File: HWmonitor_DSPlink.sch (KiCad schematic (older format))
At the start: 10 parts

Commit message: Schematic drawn!
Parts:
- removed J?: USB_B_Mini, symbol Connector:USB_B_Mini
- removed U?: FT232RL, Package_SO:SSOP-28_5.3x10.2mm_P0.65mm, symbol Interface_USB:FT232RL
- added C1, C10, C11, C12, C13, C14, C19, C20, C21, C22, C23, C28, C29, C30, C31, C32, C33, C34, C35, C5, C6: 100nF/50V, symbol Device:C
- added C15, C16, C17, C18, C2, C9: 10uF/16V, symbol Device:C
- added C24, C25, C26, C27: 68pF/50V, symbol Device:C
- added C3, C4, C7, C8: NM, symbol Device:C
- added D1, D3, D6, D7, D8: BAV99, Package_TO_SOT_SMD:SOT-23, symbol Diode:BAV99
- added D10, D5, D9: LED, symbol Device:LED
- added D11, D12, D2: D_Schottky, symbol Device:D_Schottky
- added D4: D_Zener, symbol Device:D_Zener
- added J1: USB_B_Mini, symbol Connector:USB_B_Mini
- added J3, J4, J5, J6: Conn_Coaxial, symbol Connector:Conn_Coaxial
- added L1: 0603, symbol #MyLibrary:Ferrite_Bead
- added R1, R11, R12, R13, R14, R2, R23, R24, R25, R26, R4, R5, R6, R7: 10R, symbol Device:R
- added R10: 750R, symbol Device:R
- added R15, R16, R17, R18, R19, R20, R21, R22: 10k, symbol Device:R
- added R3: 27R, symbol Device:R
- added R8, R9: 270R, symbol Device:R
- added U1: FT232RL, Package_SO:SSOP-28_5.3x10.2mm_P0.65mm, symbol Interface_USB:FT232RL
- added U10, U11, U9: OPA197xDBV, Package_TO_SOT_SMD:SOT-23-5, symbol Amplifier_Operational:OPA197xDBV
- added U5: TL431DBZ, Package_TO_SOT_SMD:SOT-23, symbol Reference_Voltage:TL431DBZ
- gave numbers to parts that had none: 8
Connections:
- net at T1.1: now also U4.3 (D2)
- net +5VA: now reaches T1.2
- net +5VA: now also U3.13 (EN2), U3.16 (VCC2), U4.2 (VCC), C1.1, C10.1, C12.1, C9.2, L1.2, R8.1, R9.1, U1.20 (VCC), U1.4 (VCCIO)
- net at T1.3: now also U4.1 (D1)
- net at T1.4: now also D12.1 (K)
- net GND: now reaches T1.5
- net GND: now also U2.15 (GND2), U2.9 (GND2), U6.7 (GND), U7.1 (GND), C11.2, C13.1, C14.1, C15.1, C16.1, C17.2, C18.1, C19.2, C20.1, C21.1, C22.1, C23.1, C24.1, C25.1, C26.1, C27.1, C28.1, C29.1, C30.1, C31.1, C32.1, C33.1, C34.1, C35.1, J3.2 (Ext), J4.2 (Ext), J5.2 (Ext), J6.2 (Ext), U5.3 (A)
- net at T1.6: now also D11.2 (A)
- net GNDA: now reaches U4.4 (GND)
- net GNDA: now also U3.15 (GND2), U3.9 (GND2), U4.5 (GND), C1.2, C10.2, C12.2, C9.1, J1.4 (ID), J1.5 (GND), J1.6 (Shield), U1.18 (GND), U1.21 (GND), U1.25 (AGND), U1.26 (TEST), U1.7 (GND)
- net at J2.1 (Pin_1): now also R3.1
- net at J2.2 (Pin_2): now also R5.1
- net at J2.3 (Pin_3): now also R1.2
- net at J2.4 (Pin_4): now also R6.1
- net at J2.6 (Pin_6): now also R7.1
- net at J2.7 (Pin_7): now also R2.2
- net GNDD: now reaches J2.8 (Pin_8)
- net GNDD: now also U2.2 (GND1), U2.8 (GND1), U3.2 (GND1), U3.8 (GND1), C2.1, C3.1, C4.1, C5.1, C6.1, C7.1, C8.1, D1.1 (K), D2.2 (A), D3.1 (K), D4.2 (A), D5.1 (K), D6.1 (K), D7.1 (K), D8.1 (K)
- net at U8.1: now also R19.1, R23.2
- net -7.5V: now reaches U8.2 (V-)
- net -7.5V: now also C17.1, C28.2, C29.2, C30.2, C31.2, D12.2 (A), U10.2 (V-), U11.2 (V-), U9.2 (V-)
- net at U8.3 (+): now also C24.2, R11.1
- net at U8.4 (-): now also R15.1, R19.2
- net +7.5V: now reaches U8.5 (V+)
- net +7.5V: now also U7.2 (VIN), C14.2, C16.2, C32.2, C33.2, C34.2, C35.2, D11.1 (K), U10.5 (V+), U11.5 (V+), U9.5 (V+)
- net VD: now reaches U3.1 (VCC1)
- net VD: now also U2.1 (VCC1), U3.4 (EN1), C2.2, C5.2, C6.2, D1.2 (A), D2.1 (K), D3.2 (A), D4.1 (K), D6.2 (A), D7.2 (A), D8.2 (A), R3.2, R4.1
- net RXD: now reaches U3.11 (OUTB)
- net RXD: now also U1.5 (RXD)
- net TXD: now reaches U3.12 (INA)
- net TXD: now also U1.1 (TXD)
- net RXD_DSP: now reaches U3.5 (OUTA)
- net RXD_DSP: now also D1.3 (K), R2.1
- net TXD_DSP: now reaches U3.6 (INB)
- net TXD_DSP: now also C8.2, D3.3 (K), R7.2
- net +5V: now reaches U2.10 (EN2)
- net +5V: now also U2.16 (VCC2), U6.1 (VDD), U7.3 (VOUT), C11.1, C18.2, C19.1, R10.2
- net SYNC: now reaches U2.12 (OUTC)
- net SYNC: now also U6.10 (SYNC)
- net SCLK: now reaches U2.13 (OUTB)
- net SCLK: now also U6.9 (SCLK)
- net DIN: now reaches U2.14 (OUTA)
- net DIN: now also U6.8 (DIN)
- net DIN_DSP: now reaches U2.3 (INA)
- net DIN_DSP: now also C3.2, D7.3 (K), R1.1
- net SCLK_DSP: now reaches U2.4 (INB)
- net SCLK_DSP: now also C4.2, D8.3 (K), R5.2
- net SYNC_DSP: now reaches U2.5 (INC)
- net SYNC_DSP: now also C7.2, D6.3 (K), R6.2
- net VOUTA: now reaches U6.2 (VOUTA)
- net VOUTA: now also R11.2, R12.2, R13.2, R14.2
- net VOUTB: now reaches U6.3 (VOUTB)
- net VOUTC: now reaches U6.4 (VOUTC)
- net REF2.5V: now reaches U6.5 (REFIN)
- net REF2.5V: now also C13.2, C15.2, C20.2, C21.2, C22.2, C23.2, R10.1, R15.2, R16.2, R17.2, R18.2, U5.1 (K), U5.2 (REF)
- net VOUTD: now reaches U6.6 (VOUTD)
- new net: J3.1 (In), R23.1
- new net: D5.2 (A), R4.2
- new net: J1.3 (D+), U1.15 (USBD+)
- new net: J1.2 (D-), U1.16 (USBD-)
- new net: J1.1 (VBUS), L1.1
- new net: D9.2 (A), R8.2
- new net: D10.2 (A), R9.2
- new net: R20.1, R24.2, U9.1
- new net: C25.2, R12.1, U9.3 (+)
- new net: R16.1, R20.2, U9.4 (-)
- new net: J4.1 (In), R24.1
- new net: R21.1, R25.2, U10.1
- new net: C26.2, R13.1, U10.3 (+)
- new net: R17.1, R21.2, U10.4 (-)
- new net: J5.1 (In), R25.1
- new net: R22.1, R26.2, U11.1
- new net: C27.2, R14.1, U11.3 (+)
- new net: R18.1, R22.2, U11.4 (-)
- new net: J6.1 (In), R26.1
- new net LED_RX: D10.1 (K), U1.22 (CBUS1)
- new net LED_TX: D9.1 (K), U1.23 (CBUS0)
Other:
- note added: "01"
- note added: "5. November 2020"
- note added: "Debug Tool"
- note added: "HWmonitor & DSPlink debug tool"
- moved on the sheet: J2, T1, U2, U3, U4, U6, U7, U8

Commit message: all footprints assigned
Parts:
- C1, C10, C11, C12, C13, C14, C19, C2, C20, C21, C22, C23, C24, C25, C26, C27, C28, C29, C3, C30, C31, C32, C33, C34, C35, C4, C5, C6, C7, C8: footprint (none) -> Capacitor_SMD:C_0603_1608Metric
- C15, C16, C17, C18, C9: footprint (none) -> Capacitor_SMD:C_0805_2012Metric
- D10, D5, D9: footprint (none) -> LED_THT:LED_D3.0mm_FlatTop
- D11, D12: footprint (none) -> Diode_SMD:D_SOD-323
- D2, D4: footprint (none) -> Diode_SMD:D_SOD-323F
- J1: footprint (none) -> Connector_USB:USB_Mini-B_Lumberg_2486_01_Horizontal
- J2: footprint (none) -> Connector_IDC:IDC-Header_2x04_P2.54mm_Vertical
- J3, J4, J5, J6: footprint (none) -> #MyLibrary:Connector_131-3701-301
- L1: footprint (none) -> Inductor_SMD:L_0603_1608Metric
- R1, R10, R11, R12, R13, R14, R15, R16, R17, R18, R19, R2, R20, R21, R22, R23, R24, R25, R26, R3, R4, R5, R6, R7, R8, R9: footprint (none) -> Resistor_SMD:R_0603_1608Metric
- T1: footprint (none) -> #MyLibrary:Wuerth_760390014
- U2, U3: footprint (none) -> #MyLibrary:SOIC-16DWW
- U4, U7: footprint (none) -> Package_TO_SOT_SMD:SOT-23-5
- U6: footprint (none) -> Package_SO:MSOP-10_3x3mm_P0.5mm

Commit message: initial placement
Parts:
- added H1, H2, H3, H4: MountingHole, MountingHole:MountingHole_3.2mm_M3, symbol Mechanical:MountingHole
- renumbered J3 to X1, J4 to X2, J5 to X3, J6 to X4
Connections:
- net VOUTA: no longer R12.2, R13.2, R14.2
- net VOUTB: now also R12.2
- net VOUTC: now also R13.2
- net VOUTD: now also R14.2
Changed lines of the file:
@@
 	13400 1200 13400 1450
 $Comp
-L Connector:Conn_Coaxial J3
+L Connector:Conn_Coaxial X1
 U 1 1 5FA672A6
 P 14850 1750
-F 0 "J3" H 14950 1725 50  0000 L CNN
+F 0 "X1" H 14950 1725 50  0000 L CNN
 F 1 "Conn_Coaxial" H 14950 1634 50  0000 L CNN
 F 2 "#MyLibrary:Connector_131-3701-301" H 14850 1750 50  0001 C CNN
@@
 	5400 2250 5400 2400
 Wire Wire Line
-	5450 1950 5100 1950
-Wire Wire Line
 	5100 1950 5100 2050
 Wire Wire Line
@@
 Wire Wire Line
 	5100 1950 3950 1950
-Connection ~ 5100 1950
 Wire Wire Line
 	3950 1850 4750 1850
@@
 	12150 3750 11850 3750
 Text Label 11850 3750 0    50   ~ 0
-VOUTA
+VOUTB
 Wire Wire Line
 	14500 3850 14650 3850
@@
 	13400 3300 13400 3550
 $Comp
-L Connector:Conn_Coaxial J4
+L Connector:Conn_Coaxial X2
 U 1 1 61F80535
 P 14850 3850
-F 0 "J4" H 14950 3825 50  0000 L CNN
+F 0 "X2" H 14950 3825 50  0000 L CNN
 F 1 "Conn_Coaxial" H 14950 3734 50  0000 L CNN
 F 2 "#MyLibrary:Connector_131-3701-301" H 14850 3850 50  0001 C CNN
@@
 	12150 5850 11850 5850
 Text Label 11850 5850 0    50   ~ 0
-VOUTA
+VOUTC
 Wire Wire Line
 	14500 5950 14650 5950
@@
 	13400 5400 13400 5650
 $Comp
-L Connector:Conn_Coaxial J5
+L Connector:Conn_Coaxial X3
 U 1 1 61FBE922
 P 14850 5950
-F 0 "J5" H 14950 5925 50  0000 L CNN
+F 0 "X3" H 14950 5925 50  0000 L CNN
 F 1 "Conn_Coaxial" H 14950 5834 50  0000 L CNN
 F 2 "#MyLibrary:Connector_131-3701-301" H 14850 5950 50  0001 C CNN
@@
 	12150 8000 11850 8000
 Text Label 11850 8000 0    50   ~ 0
-VOUTA
+VOUTD
 Wire Wire Line
 	14500 8100 14650 8100
@@
 	13400 7550 13400 7800
 $Comp
-L Connector:Conn_Coaxial J6
+L Connector:Conn_Coaxial X4
 U 1 1 61FBE9AB
 P 14850 8100
-F 0 "J6" H 14950 8075 50  0000 L CNN
+F 0 "X4" H 14950 8075 50  0000 L CNN
 F 1 "Conn_Coaxial" H 14950 7984 50  0000 L CNN
 F 2 "#MyLibrary:Connector_131-3701-301" H 14850 8100 50  0001 C CNN
@@
 	1    0    0    -1
 $EndComp
+Wire Wire Line
+	5100 1950 5450 1950
+Connection ~ 5100 1950
+$Comp
+L Mechanical:MountingHole H1
+U 1 1 5FCFB9B1
+P 10950 10100
+F 0 "H1" H 11050 10146 50  0000 L CNN
+F 1 "MountingHole" H 11050 10055 50  0000 L CNN
+F 2 "MountingHole:MountingHole_3.2mm_M3" H 10950 10100 50  0001 C CNN
+F 3 "~" H 10950 10100 50  0001 C CNN
+	1    10950 10100
+	1    0    0    -1
+$EndComp
+$Comp
+L Mechanical:MountingHole H2
+U 1 1 5FCFCB0C
+P 10950 10300
+F 0 "H2" H 11050 10346 50  0000 L CNN
+F 1 "MountingHole" H 11050 10255 50  0000 L CNN
+F 2 "MountingHole:MountingHole_3.2mm_M3" H 10950 10300 50  0001 C CNN
+F 3 "~" H 10950 10300 50  0001 C CNN
+	1    10950 10300
+	1    0    0    -1
+$EndComp
+$Comp
+L Mechanical:MountingHole H3
+U 1 1 5FCFDAD4
+P 10950 10500
+F 0 "H3" H 11050 10546 50  0000 L CNN
+F 1 "MountingHole" H 11050 10455 50  0000 L CNN
+F 2 "MountingHole:MountingHole_3.2mm_M3" H 10950 10500 50  0001 C CNN
+F 3 "~" H 10950 10500 50  0001 C CNN
+	1    10950 10500
+	1    0    0    -1
+$EndComp
+$Comp
+L Mechanical:MountingHole H4
+U 1 1 5FCFEBB5
+P 10950 10700
+F 0 "H4" H 11050 10746 50  0000 L CNN
+F 1 "MountingHole" H 11050 10655 50  0000 L CNN
+F 2 "MountingHole:MountingHole_3.2mm_M3" H 10950 10700 50  0001 C CNN
+F 3 "~" H 10950 10700 50  0001 C CNN
+	1    10950 10700
+	1    0    0    -1
+$EndComp

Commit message: placement, added USB input protection
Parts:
- added R27, R28: 47R, Resistor_SMD:R_0603_1608Metric, symbol Device:R
- added U12: USBLC6-2SC6, Package_TO_SOT_SMD:SOT-23-6, symbol Power_Protection:USBLC6-2SC6
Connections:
- net +5VA: now also C1.2, U12.5 (VBUS); no longer C1.1
- net GNDA: now also C1.1, U12.2 (GND); no longer C1.2
- net at U1.15 (USBD+): now also R27.1; no longer J1.3 (D+)
- net at U1.16 (USBD-): now also R28.1; no longer J1.2 (D-)
- new net: J1.2 (D-), U12.4 (I/O2)
- new net: J1.3 (D+), U12.6 (I/O1)
- new net USBD+: R27.2, U12.1 (I/O1)
- new net USBD-: R28.2, U12.3 (I/O2)
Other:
- moved on the sheet: C1, J1, L1, U1

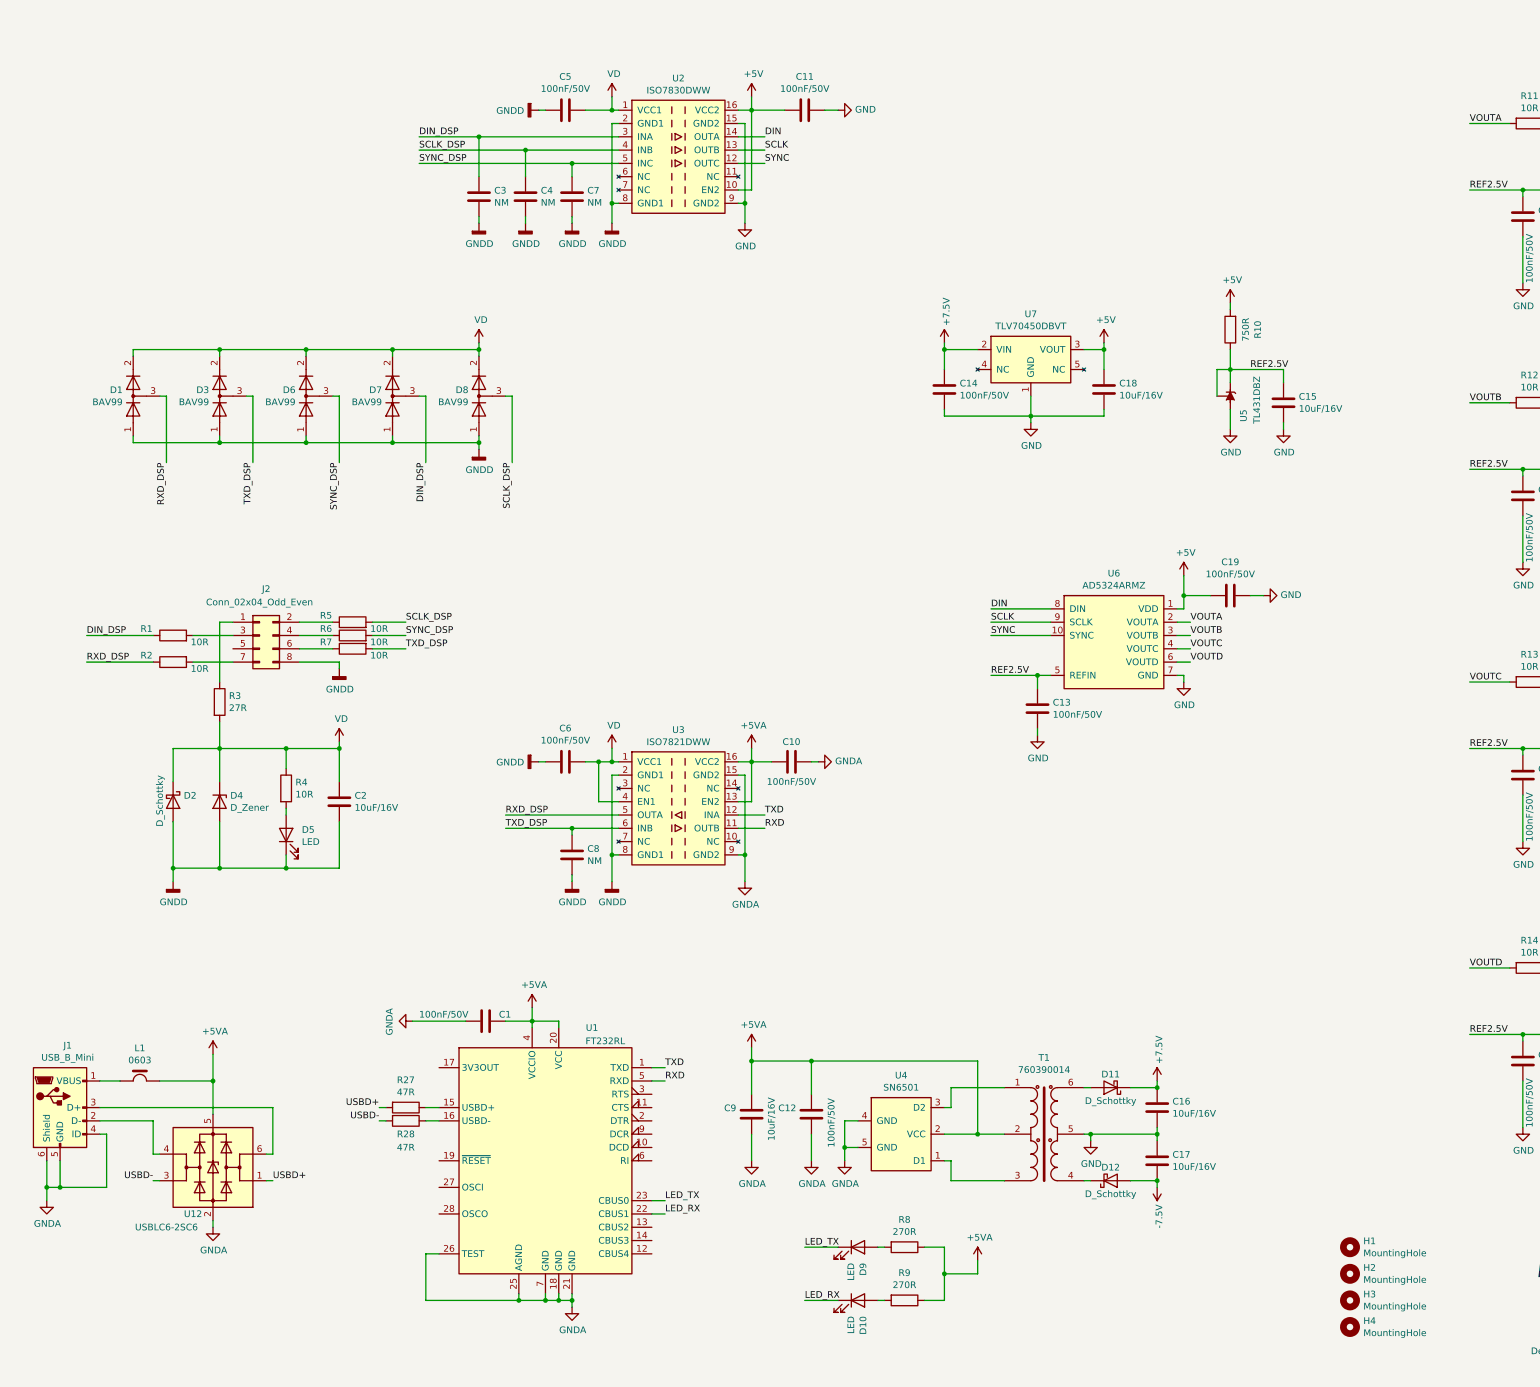
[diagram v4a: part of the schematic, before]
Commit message: routing finished, added all MPNs
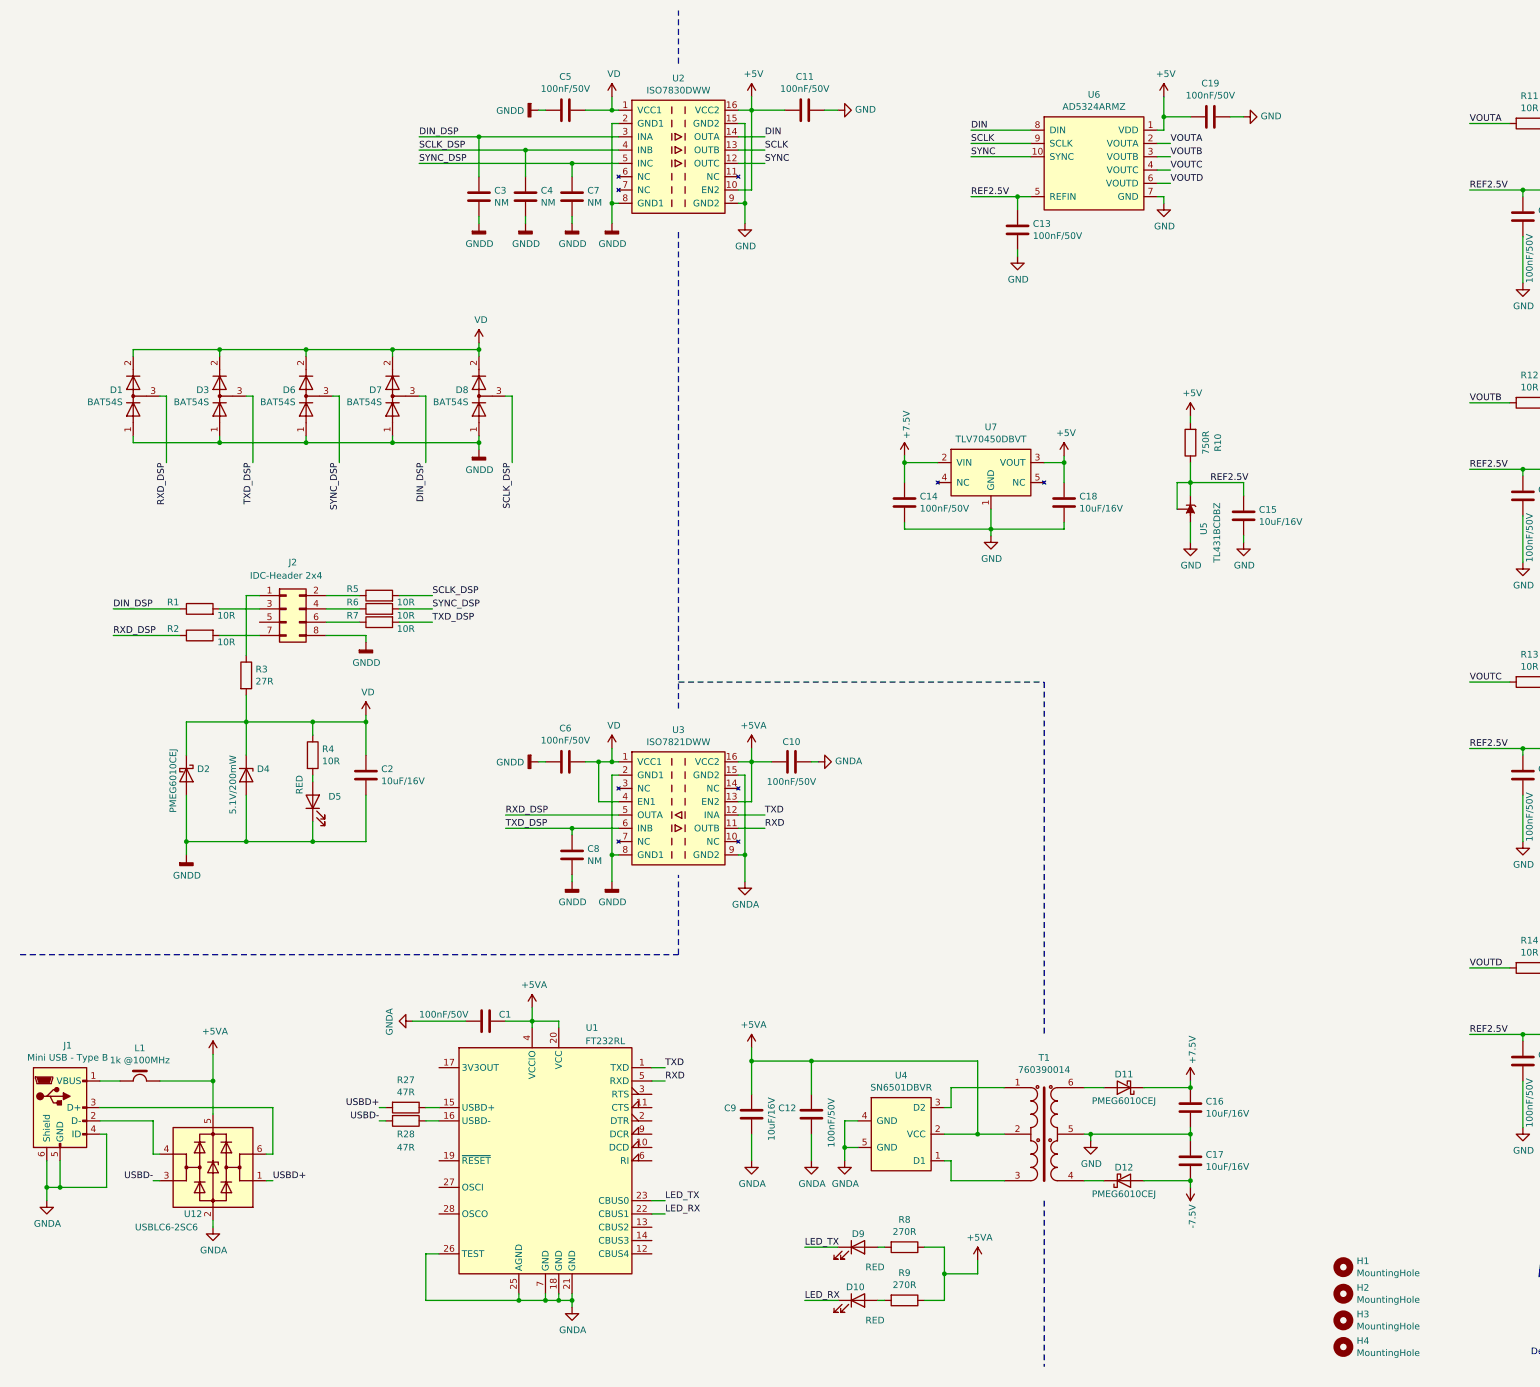
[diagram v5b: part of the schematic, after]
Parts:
- C15, C16, C17, C18, C9: MPN (none) -> CC0805MKX7R7BB106
- C2: footprint Capacitor_SMD:C_0603_1608Metric -> Capacitor_SMD:C_0805_2012Metric; MPN (none) -> CC0805MKX7R7BB106
- D1, D3, D6, D7, D8: value BAV99 -> BAT54S; MPN (none) -> BAT54S
- D10, D5, D9: value LED -> RED; MPN (none) -> WP424SRDT
- D11, D12: value D_Schottky -> PMEG6010CEJ; footprint Diode_SMD:D_SOD-323 -> Diode_SMD:D_SOD-323F; MPN (none) -> PMEG6010CEJ
- D2: value D_Schottky -> PMEG6010CEJ; MPN (none) -> PMEG6010CEJ
- D4: value D_Zener -> 5.1V/200mW; MPN (none) -> MM3Z5V1C
- H1, H2, H3, H4: MPN (none) -> PHANTOM
- J1: value USB_B_Mini -> Mini USB - Type B; MPN (none) -> 65100516121
- J2: value Conn_02x04_Odd_Even -> IDC-Header 2x4; MPN (none) -> 61200821621
- L1: value 0603 -> 1k @100MHz; MPN (none) -> 742792664
- T1: MPN (none) -> 760390014
- U1: MPN (none) -> FT232RL
- U10, U11, U8, U9: MPN (none) -> OPA197IDBV
- U12: MPN (none) -> USBLC6-2SC6
- U2: MPN (none) -> ISO7830DWW
- U3: MPN (none) -> ISO7821DWW
- U4: value SN6501 -> SN6501DBVR; MPN (none) -> SN6501DBVR
- U5: value TL431DBZ -> TL431BCDBZ; MPN (none) -> TL431BCDBZ
- U6: MPN (none) -> AD5324ARMZ
- U7: MPN (none) -> TLV70450DBVT
- X1, X2, X3, X4: MPN (none) -> 131-3701-301
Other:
- moved on the sheet: C13, C14, C15, C16, C17, C18, C19, C2, D11, D12, D2, D4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
